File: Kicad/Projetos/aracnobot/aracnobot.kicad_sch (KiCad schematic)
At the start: 1 part, among them U1 SC0195_9_

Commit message: Kicad atualaizao footprint e schematico
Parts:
- added M1: Motor_Servo, Connector_PinHeader_2.54mm:PinHeader_1x03_P2.54mm_Vertical, symbol Motor:Motor_Servo
- added U2: DEVKIT_V1_ESP32-WROOM-32, DEVKIT_V1_ESP32-WROOM-32:MODULE_DEVKIT_V1_ESP32-WROOM-32, symbol DEVKIT_V1_ESP32-WROOM-32:DEVKIT_V1_ESP32-WROOM-32
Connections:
- net GND: now also U2.2 (GND), U2.29 (GND)
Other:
- moved on the sheet: U1

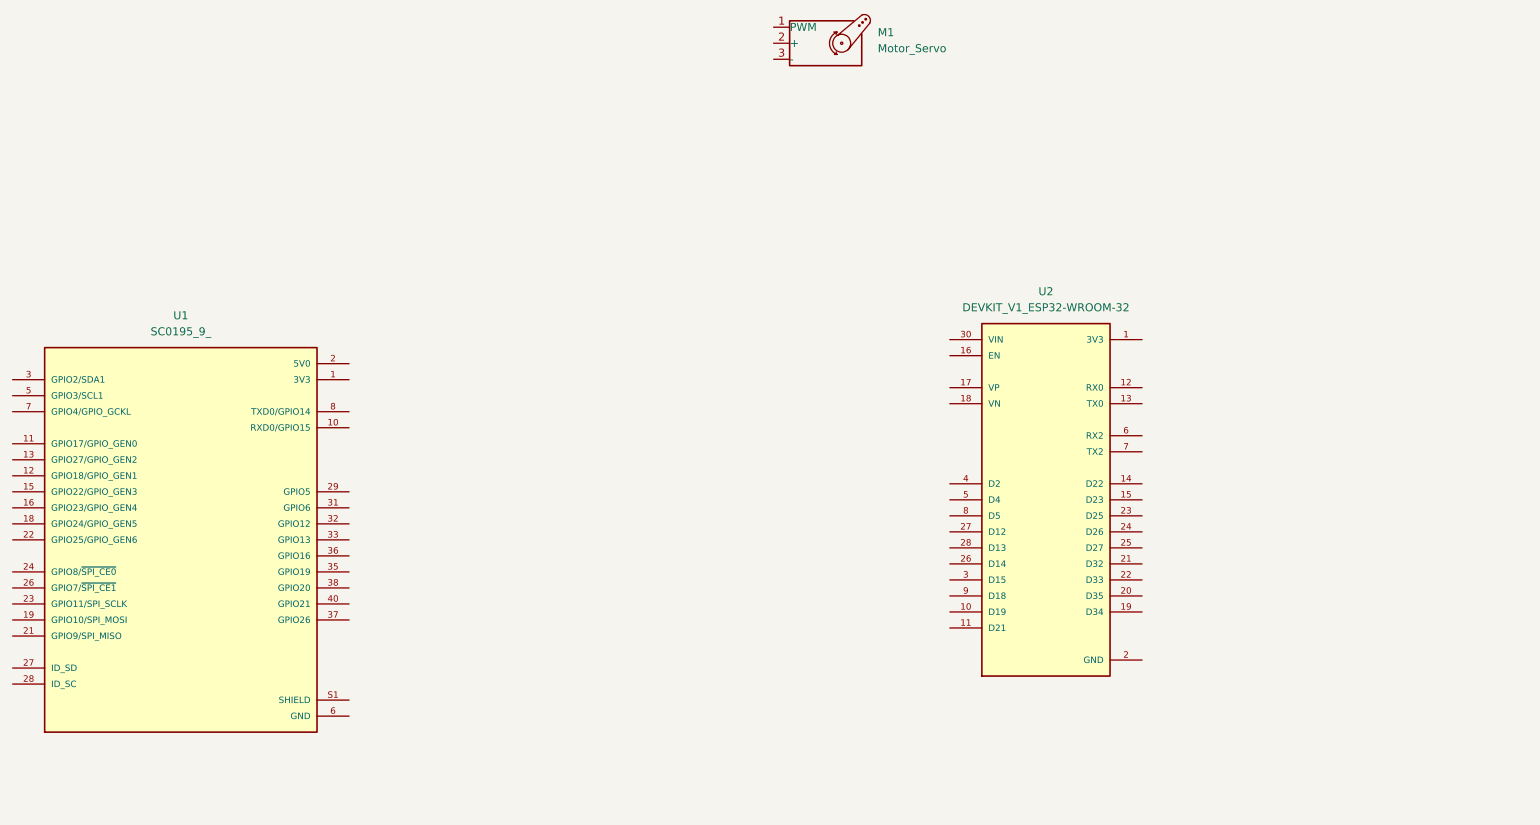
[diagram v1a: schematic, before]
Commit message: kicad atualizacao, servo motores
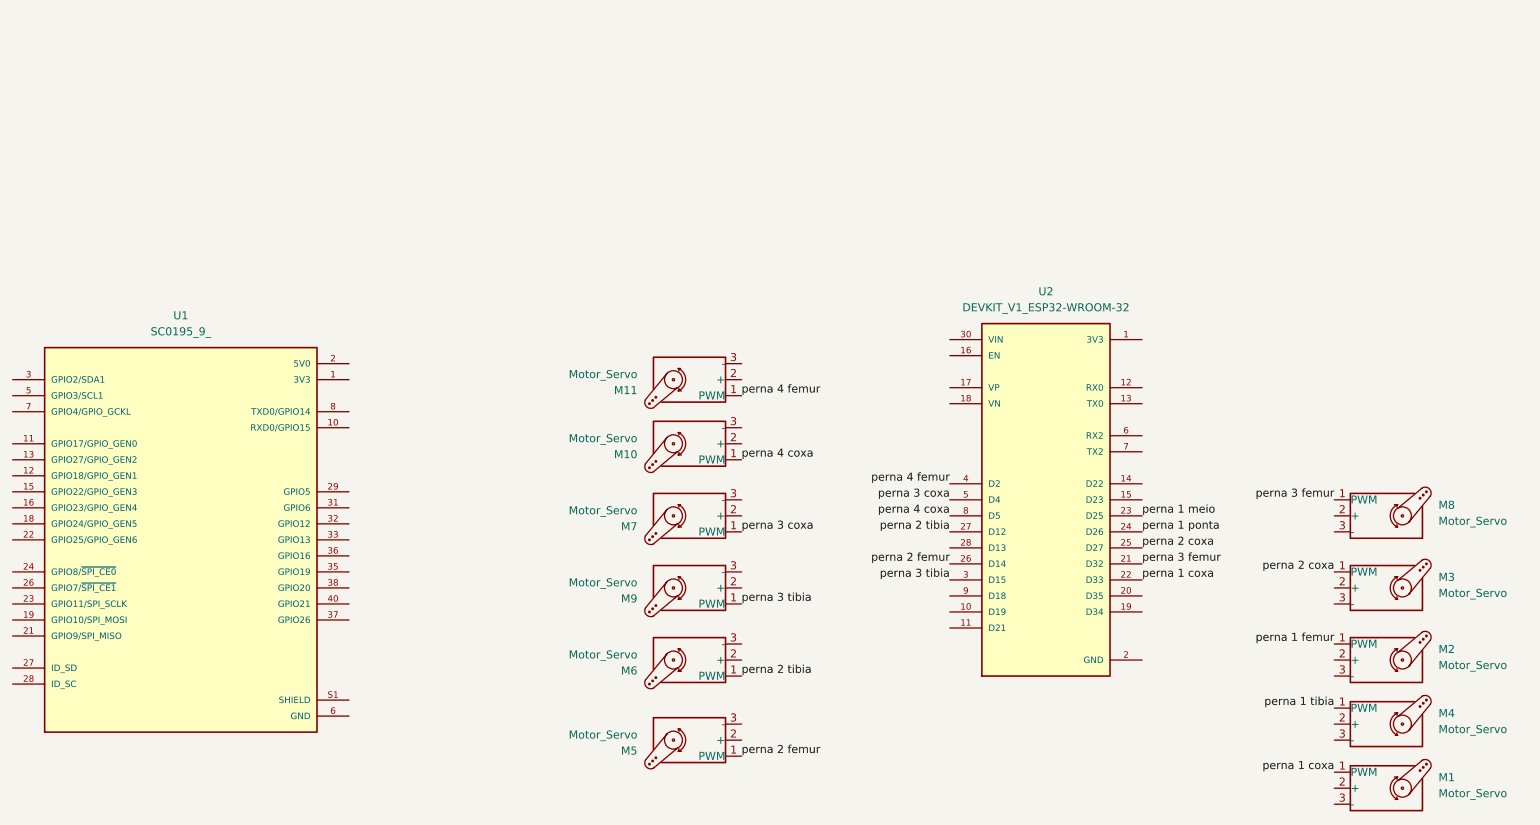
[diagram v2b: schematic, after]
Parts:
- added M10, M11, M2, M3, M4, M5, M6, M7, M8, M9: Motor_Servo, Connector_PinHeader_2.54mm:PinHeader_1x03_P2.54mm_Vertical, symbol Motor:Motor_Servo
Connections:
- net perna 3 femur: now reaches U2.21 (D32)
- net perna 3 femur: now also M8.1 (PWM)
- net perna 1 coxa: now reaches U2.22 (D33)
- net perna 1 coxa: now also M1.1 (PWM)
- net perna 1 meio: now reaches U2.23 (D25)
- net perna 1 ponta: now reaches U2.24 (D26)
- net perna 2 coxa: now reaches U2.25 (D27)
- net perna 2 coxa: now also M3.1 (PWM)
- net perna 2 femur: now reaches U2.26 (D14)
- net perna 2 femur: now also M5.1 (PWM)
- net perna 2 tibia: now reaches U2.27 (D12)
- net perna 2 tibia: now also M6.1 (PWM)
- net perna 3 tibia: now reaches U2.3 (D15)
- net perna 3 tibia: now also M9.1 (PWM)
- net perna 4 femur: now reaches U2.4 (D2)
- net perna 4 femur: now also M11.1 (PWM)
- net perna 3 coxa: now reaches U2.5 (D4)
- net perna 3 coxa: now also M7.1 (PWM)
- net perna 4 coxa: now reaches U2.8 (D5)
- net perna 4 coxa: now also M10.1 (PWM)
- new net perna 1 femur: M2.1 (PWM)
- new net perna 1 tibia: M4.1 (PWM)
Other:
- moved on the sheet: M1
